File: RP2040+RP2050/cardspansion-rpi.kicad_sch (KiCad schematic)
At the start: 4 parts, among them J1 M2-E 2230, U1 RP2350-Tiny

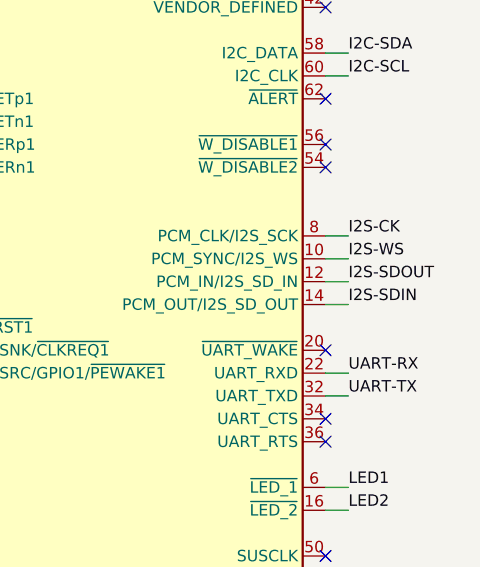
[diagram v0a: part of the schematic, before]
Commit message: Fix cardspansion-rpi I2S wiring
I2S-SDIN and I2S-SDOUT nets were switched around
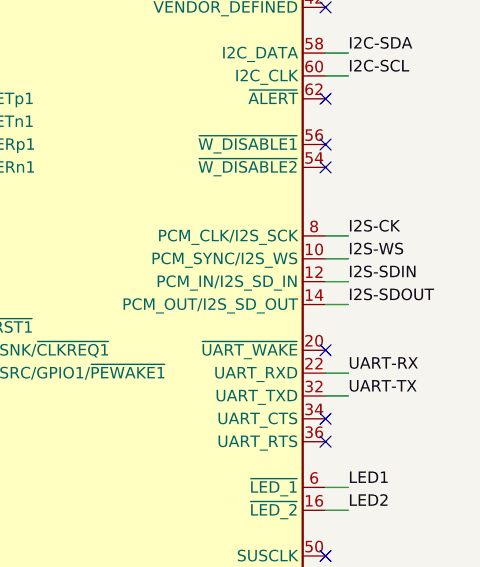
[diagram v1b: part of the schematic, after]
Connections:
- net I2S-SDIN: now also J1.12 (PCM_IN/I2S_SD_IN); no longer J1.14 (PCM_OUT/I2S_SD_OUT)
- net I2S-SDOUT: now also J1.14 (PCM_OUT/I2S_SD_OUT); no longer J1.12 (PCM_IN/I2S_SD_IN)
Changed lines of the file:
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@@
-		)
-	)
-	(label "I2S-SDIN"
-		(at 162.56 73.66 0)
-		(effects
-			(font
-				(size 1.27 1.27)
-			)
-			(justify left bottom)
 		)
 	)
 	(label "I2S-SDOUT"
-		(at 162.56 71.12 0)
+		(at 162.56 73.66 0)
 		(effects
 			(font
@@
 		)
 	)
+	(label "I2S-SDIN"
+		(at 162.56 71.12 0)
+		(effects
+			(font
+				(size 1.27 1.27)
+			)
+			(justify left bottom)
+		)
+	)
